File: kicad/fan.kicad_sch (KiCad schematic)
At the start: 3 parts, among them M1 Fan, Q6 AO3400A

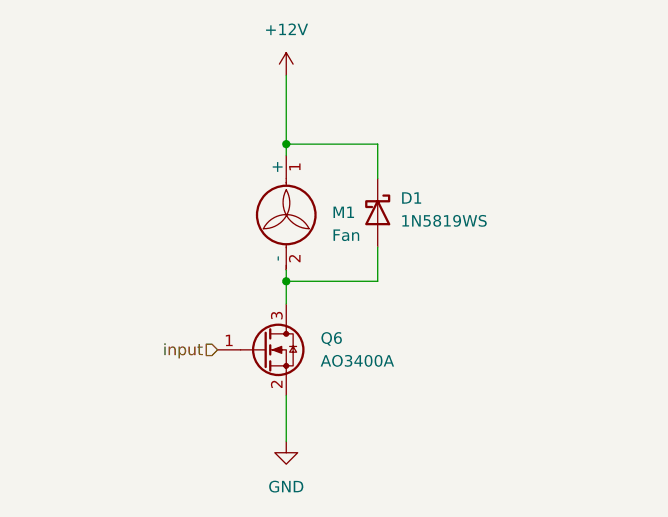
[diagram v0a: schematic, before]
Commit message: added connectors to schematic
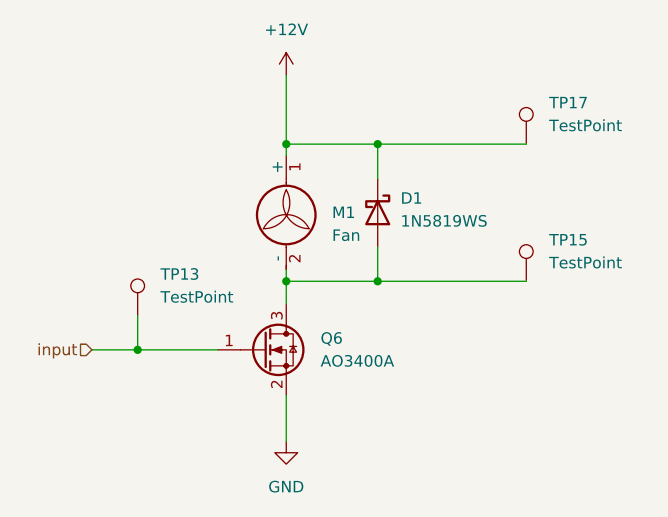
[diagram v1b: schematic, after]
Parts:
- added TP13, TP15, TP17: TestPoint, symbol Connector:TestPoint
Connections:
- net +12V: now also TP17.1
- net input: now also TP13.1
- net at D1.2 (A), M1.2 (-), Q6.3 (D): now also TP15.1

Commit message: added footprints
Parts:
- TP13, TP15, TP17: footprint (none) -> TestPoint:TestPoint_Pad_D2.5mm
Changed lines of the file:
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@@
 			)
 		)
-		(property "Footprint" ""
+		(property "Footprint" "TestPoint:TestPoint_Pad_D2.5mm"
 			(at 110.49 96.52 0)
 			(effects
@@
 			)
 		)
-		(property "Footprint" ""
+		(property "Footprint" "TestPoint:TestPoint_Pad_D2.5mm"
 			(at 153.67 92.71 0)
 			(effects
@@
 			)
 		)
-		(property "Footprint" ""
+		(property "Footprint" "TestPoint:TestPoint_Pad_D2.5mm"
 			(at 153.67 77.47 0)
 			(effects

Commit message: pcb design v0.2
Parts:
- removed TP17: TestPoint, TestPoint:TestPoint_Pad_D2.5mm, symbol Connector:TestPoint
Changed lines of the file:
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@@
 		(color 0 0 0 0)
 	)
-	(junction
-		(at 132.08 77.47)
-		(diameter 0)
-		(color 0 0 0 0)
-	)
 	(wire
 		(pts
@@
 		(pts
 			(xy 121.92 69.85) (xy 121.92 77.47)
-		)
-		(stroke
-			(width 0)
-			(type default)
-		)
-	)
-	(wire
-		(pts
-			(xy 132.08 77.47) (xy 148.59 77.47)
 		)
 		(stroke
@@
 					(unit 1)
 				)
-			)
-		)
-	)
-	(symbol
-		(lib_id "Connector:TestPoint")
-		(at 148.59 77.47 0)
-		(unit 1)
-		(exclude_from_sim no)
-		(in_bom yes)
-		(on_board yes)
-		(dnp no)
-		(fields_autoplaced yes)
-		(property "Reference" "TP17"
-			(at 151.13 72.8979 0)
-			(effects
-				(font
-					(size 1.27 1.27)
-				)
-				(justify left)
-			)
-		)
-		(property "Value" "TestPoint"
-			(at 151.13 75.4379 0)
-			(effects
-				(font
-					(size 1.27 1.27)
-				)
-				(justify left)
-			)
-		)
-		(property "Footprint" "TestPoint:TestPoint_Pad_D2.5mm"
-			(at 153.67 77.47 0)
-			(effects
-				(font
-					(size 1.27 1.27)
-				)
-				(hide yes)
-			)
-		)
-		(property "Datasheet" "~"
-			(at 153.67 77.47 0)
-			(effects
-				(font
-					(size 1.27 1.27)
-				)
-				(hide yes)
-			)
-		)
-		(property "Description" "test point"
-			(at 148.59 77.47 0)
-			(effects
-				(font
-					(size 1.27 1.27)
-				)
-				(hide yes)
-			)
-		)
-		(pin "1"
-		)
-		(instances
-			(project "closed-drybox"
-				(path "/99399f2a-756c-4718-9b6a-bb37855e6538/2234efbe-ebbf-4aab-bbfd-018f77cfe3a5"
-					(reference "TP18")
-					(unit 1)
-				)
-				(path "/99399f2a-756c-4718-9b6a-bb37855e6538/2668133d-2aed-41c2-9473-f2895de6f795"
-					(reference "TP17")
-					(unit 1)
-				)

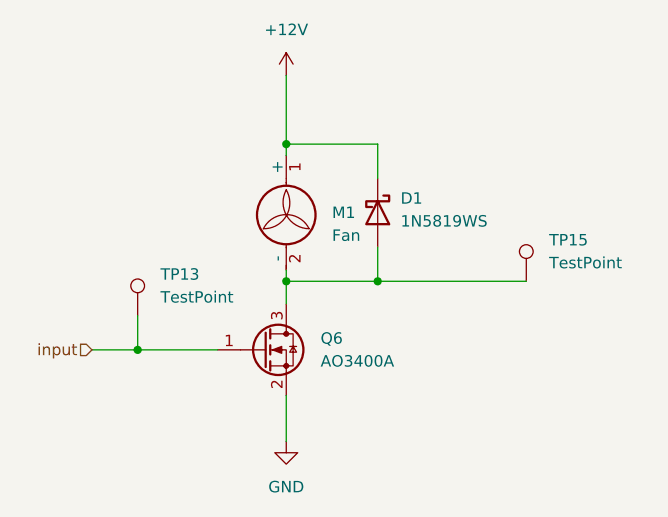
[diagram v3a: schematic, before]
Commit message: change routing, fix capactitors, add pulldown resistors
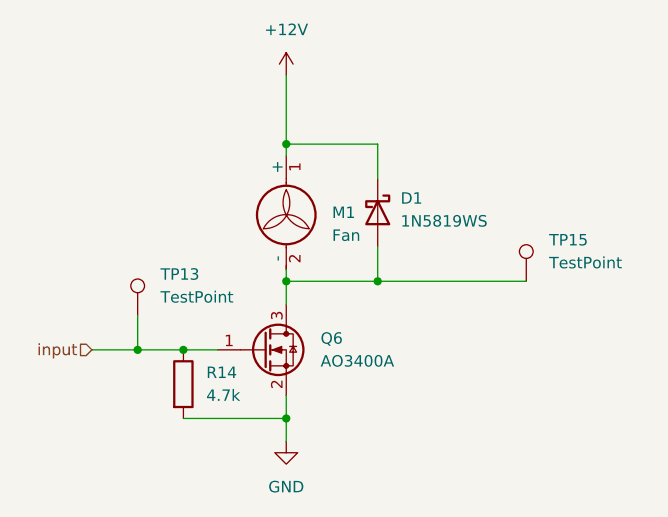
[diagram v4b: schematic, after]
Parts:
- added R14: 4.7k, Resistor_SMD:R_0603_1608Metric_Pad0.98x0.95mm_HandSolder, symbol Device:R
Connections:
- net GND: now also R14.2
- net input: now also R14.1
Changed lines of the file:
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@@
+	)
+	(junction
+		(at 110.49 100.33)
+		(diameter 0)
+		(color 0 0 0 0)
+	)
+	(junction
+		(at 121.92 107.95)
+		(diameter 0)
+		(color 0 0 0 0)
 	)
 	(junction
@@
 	(wire
 		(pts
-			(xy 105.41 100.33) (xy 114.3 100.33)
+			(xy 110.49 107.95) (xy 121.92 107.95)
+		)
+		(stroke
+			(width 0)
+			(type default)
+		)
+	)
+	(wire
+		(pts
+			(xy 105.41 100.33) (xy 110.49 100.33)
+		)
+		(stroke
+			(width 0)
+			(type default)
+		)
+	)
+	(wire
+		(pts
+			(xy 110.49 100.33) (xy 114.3 100.33)
 		)
 		(stroke
@@
 	(wire
 		(pts
+			(xy 121.92 107.95) (xy 121.92 110.49)
+		)
+		(stroke
+			(width 0)
+			(type default)
+		)
+	)
+	(wire
+		(pts
 			(xy 132.08 92.71) (xy 148.59 92.71)
 		)
@@
 	(wire
 		(pts
-			(xy 121.92 105.41) (xy 121.92 110.49)
+			(xy 121.92 105.41) (xy 121.92 107.95)
 		)
 		(stroke
@@
 					(unit 1)
 				)
+			)
+		)
+	)
+	(symbol
+		(lib_id "Device:R")
+		(at 110.49 104.14 0)
+		(unit 1)
+		(exclude_from_sim no)
+		(in_bom yes)
+		(on_board yes)
+		(dnp no)
+		(fields_autoplaced yes)
+		(property "Reference" "R14"
+			(at 113.03 102.8699 0)
+			(effects
+				(font
+					(size 1.27 1.27)
+				)
+				(justify left)
+			)
+		)
+		(property "Value" "4.7k"
+			(at 113.03 105.4099 0)
+			(effects
+				(font
+					(size 1.27 1.27)
+				)
+				(justify left)
+			)
+		)
+		(property "Footprint" "Resistor_SMD:R_0603_1608Metric_Pad0.98x0.95mm_HandSolder"
+			(at 108.712 104.14 90)
+			(effects
+				(font
+					(size 1.27 1.27)
+				)
+				(hide yes)
+			)
+		)
+		(property "Datasheet" "~"
+			(at 110.49 104.14 0)
+			(effects
+				(font
+					(size 1.27 1.27)
+				)
+				(hide yes)
+			)
+		)
+		(property "Description" "Resistor"
+			(at 110.49 104.14 0)
+			(effects
+				(font
+					(size 1.27 1.27)
+				)
+				(hide yes)
+			)
+		)
+		(pin "2"
+		)
+		(pin "1"
+		)
+		(instances
+			(project "closed-drybox"
+				(path "/99399f2a-756c-4718-9b6a-bb37855e6538/2234efbe-ebbf-4aab-bbfd-018f77cfe3a5"
+					(reference "R15")
+					(unit 1)
+				)
+				(path "/99399f2a-756c-4718-9b6a-bb37855e6538/2668133d-2aed-41c2-9473-f2895de6f795"
+					(reference "R14")
+					(unit 1)
+				)

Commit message: set LCSC ID's
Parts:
- M1: LCSC C158012 -> C157931
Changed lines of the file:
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@@
 			)
 		)
-		(property "LCSC" "C158012"
+		(property "LCSC" "C157931"
 			(at 127 85.0899 0)
 			(effects
